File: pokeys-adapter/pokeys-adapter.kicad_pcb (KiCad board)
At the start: 2 copper layers, 19 x 62.9 mm, 7 parts, among them J1 Bus, J2 PinHeader_01x12, J3 PinHeader_01x12, J4 Screw_Terminal_01x02, J5 Mounting hole, J6 Mounting hole

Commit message: Minor artistic changes
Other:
- board text added: "CNC Panel Adapter Hacklab Lahti"

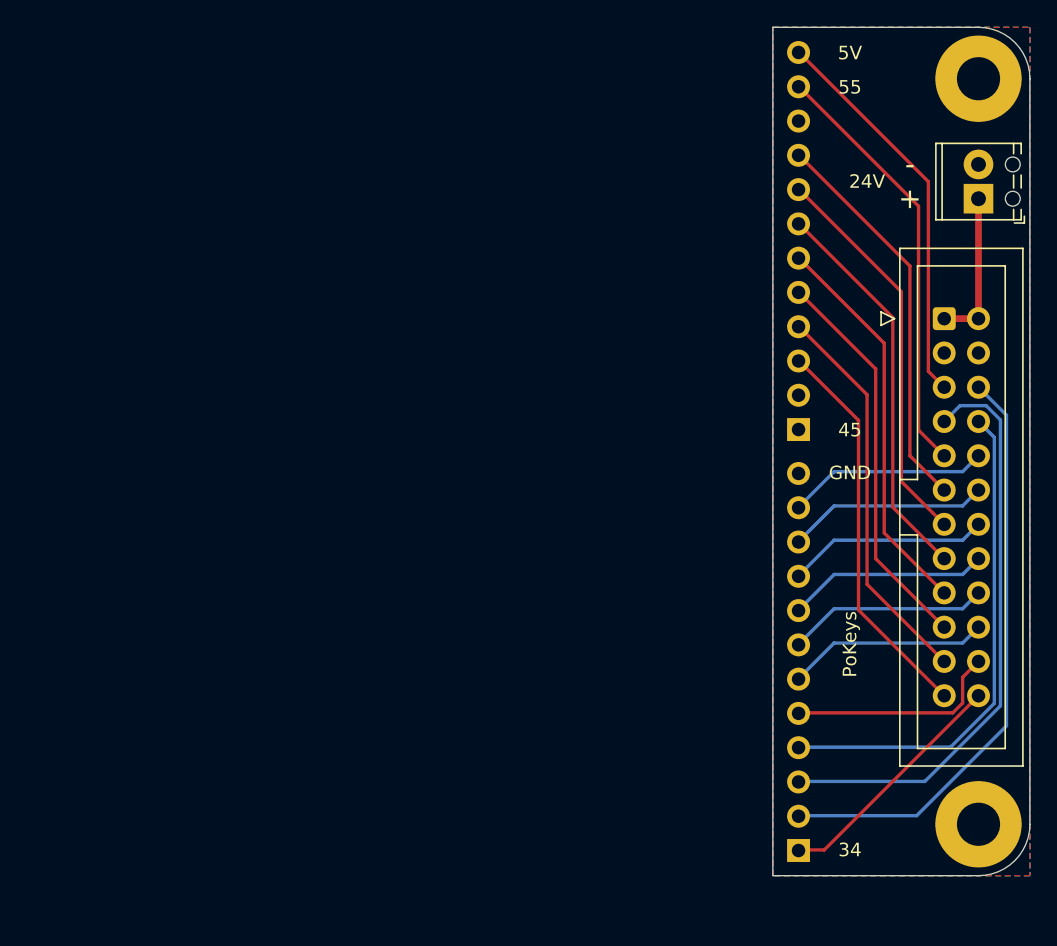
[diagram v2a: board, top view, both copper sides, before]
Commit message: Add level shifters and pullups
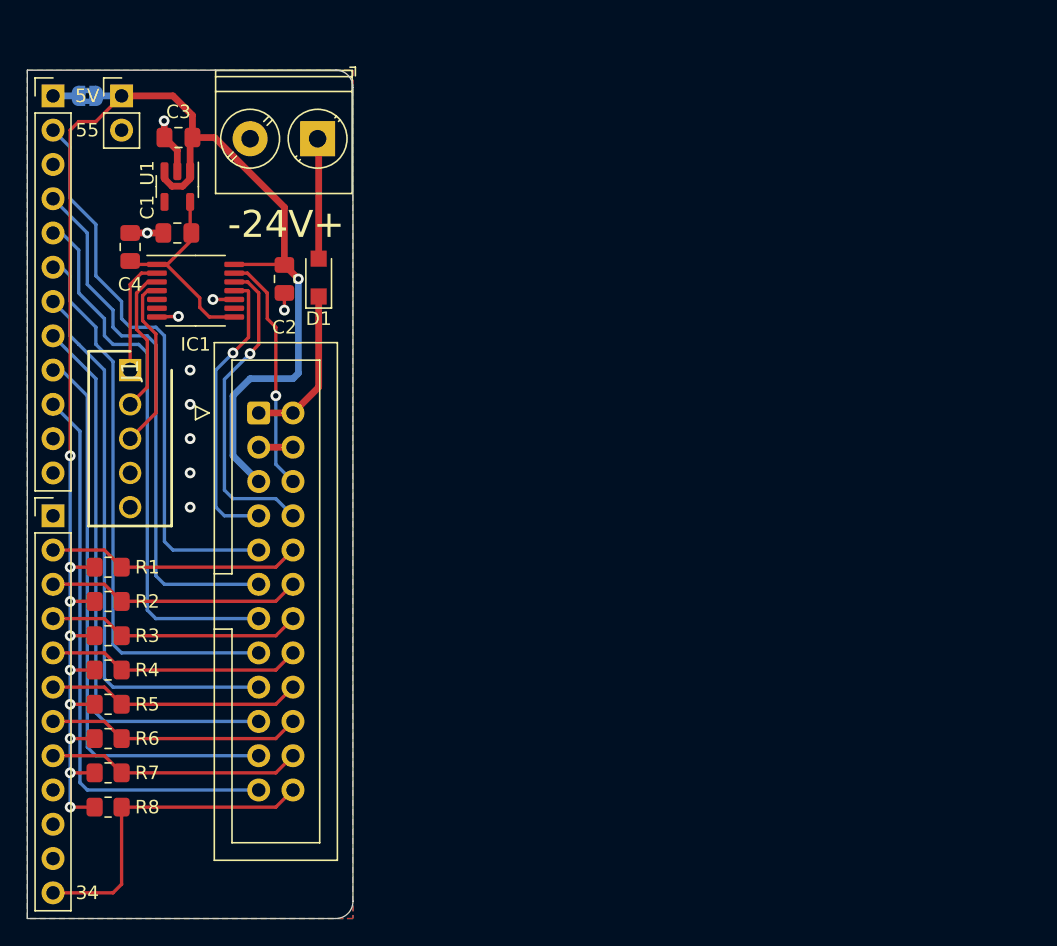
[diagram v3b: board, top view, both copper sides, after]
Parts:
- removed the J5 at (96.5, 22.9)
- removed the J6 at (96.5, 78.1)
- removed REF**: Pokeys56U, Project:Pokeys56U
- added C1: 0.1u, Capacitor_SMD:C_0805_2012Metric_Pad1.18x1.45mm_HandSolder, F.Cu at (33.7, 35.3)
- added C2: 0.1u, Capacitor_SMD:C_0805_2012Metric_Pad1.18x1.45mm_HandSolder, F.Cu at (45.1, 37.7)
- added C3: 1u, Capacitor_SMD:C_0805_2012Metric_Pad1.18x1.45mm_HandSolder, F.Cu at (37.2, 27.2)
- added C4: 1u, Capacitor_SMD:C_0805_2012Metric_Pad1.18x1.45mm_HandSolder, F.Cu at (37.1, 34.3)
- added D1: PMEG3020BER, Diode_SMD:Nexperia_CFP3_SOD-123W, F.Cu at (47.6, 37.6)
- added IC1: TXU0304PWR, Package_SO:TSSOP-14_4.4x5mm_P0.65mm, F.Cu at (38.5, 38.6)
- added J1: 22-27-2051, Project:HDRV5W64P0X254_1X5_1270X580X1205P, F.Cu at (33.7, 44.5)
- added J4: Conn_01x02_Male, Connector_PinHeader_2.54mm:PinHeader_1x02_P2.54mm_Vertical, F.Cu at (33.0, 24.1)
- added JP1: SolderJumper_2_Bridged, Jumper:SolderJumper-2_P1.3mm_Bridged2Bar_RoundedPad1.0x1.5mm, B.Cu at (30.5, 24.1)
- added R1: 1k, Resistor_SMD:R_0805_2012Metric_Pad1.20x1.40mm_HandSolder, F.Cu at (32.0, 59.1)
- added R2: 1k, Resistor_SMD:R_0805_2012Metric_Pad1.20x1.40mm_HandSolder, F.Cu at (32.0, 61.6)
- added R3: 1k, Resistor_SMD:R_0805_2012Metric_Pad1.20x1.40mm_HandSolder, F.Cu at (32.0, 64.1)
- added R4: 1k, Resistor_SMD:R_0805_2012Metric_Pad1.20x1.40mm_HandSolder, F.Cu at (32.0, 66.7)
- added R5: 1k, Resistor_SMD:R_0805_2012Metric_Pad1.20x1.40mm_HandSolder, F.Cu at (32.0, 69.2)
- added R6: 1k, Resistor_SMD:R_0805_2012Metric_Pad1.20x1.40mm_HandSolder, F.Cu at (32.0, 71.8)
- added R7: 1k, Resistor_SMD:R_0805_2012Metric_Pad1.20x1.40mm_HandSolder, F.Cu at (32.0, 74.3)
- added R8: 1k, Resistor_SMD:R_0805_2012Metric_Pad1.20x1.40mm_HandSolder, F.Cu at (32.0, 76.8)
- added U1: MIC5504-3.3YM5, Package_TO_SOT_SMD:SOT-23-5, F.Cu at (37.1, 30.9)
- J2, J3: footprint Project:PinHeader_1x12_P2.54mm_Horizontal_Reversed -> Connector_PinHeader_2.54mm:PinHeader_1x12_P2.54mm_Vertical
- J6: renamed from J4; footprint Project:TerminalBlock_Phoenix_MPT-0,5-2-2.54_1x02_P2.54mm_Horizontal -> TerminalBlock_Phoenix:TerminalBlock_Phoenix_PT-1,5-2-5.0-H_1x02_P5.00mm_Horizontal
- moved J3 60.6 mm to (27.9, 55.2), turned to 0 degrees
- moved J2 60.5 mm to (27.9, 24.1), turned to 0 degrees
- moved J5 51.3 mm to (43.2, 47.6)
- moved J6 49.2 mm to (47.5, 27.3), turned to 180 degrees
- renumbered J1 to J5
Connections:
- J2 pad 10: Net-(J2-Pad10) -> /R8
- J2 pad 11: /R1 -> unconnected-(J2-Pad11)
- J2 pad 12: +5V -> unconnected-(J2-Pad12)
- J2 pad 2: Net-(J2-Pad2) -> /R1
- J2 pad 3: /R8 -> unconnected-(J2-Pad3)
- J2 pad 4: /R7 -> /R2
- J2 pad 5: /R6 -> /R3
- J2 pad 6: /R5 -> /R4
- J2 pad 7: /R4 -> /R5
- J2 pad 8: /R3 -> /R6
- J2 pad 9: /R2 -> /R7
- J3 pad 1: /C8 -> GND
- J3 pad 10: /C2 -> unconnected-(J3-Pad10)
- J3 pad 11: /C1 -> unconnected-(J3-Pad11)
- J3 pad 12: GND -> /C8
- J3 pad 2: /BusClock -> /C1
- J3 pad 3: /BusOut -> /C2
- J3 pad 4: /BusLatch -> /C3
- J3 pad 5: /C7 -> /C4
- J3 pad 6: /C6 -> /C5
- J3 pad 7: /C5 -> /C6
- J3 pad 8: /C4 -> /C7
- J3 pad 9: /C3 -> unconnected-(J3-Pad9)
- J6 pad 1: +24V -> Net-(D1-Pad2)
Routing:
- net +5V: track 29.3 -> 123.0 mm, vias 0 -> 10
- net /BusClock: track 44.1 -> 17.8 mm, vias 0 -> 1
- net /BusOut: track 43.6 -> 21.5 mm, vias 0 -> 1
- net +3V3: track 0.00 -> 15.3 mm
- net GND: track 0.00 -> 13.7 mm, vias 0 -> 10
- net /BusLatch: track 37.2 -> 23.7 mm, vias 0 -> 1
- net /R8: track 29.3 -> 42.3 mm
- net Net-(IC1-Pad4): track 0.00 -> 13.0 mm
- net /R7: track 29.3 -> 41.7 mm
- net /R6: track 29.3 -> 41.6 mm
- net /R5: track 29.3 -> 41.2 mm
- net /R4: track 29.3 -> 40.6 mm
- net Net-(IC1-Pad3): track 0.00 -> 11.0 mm
- net /R3: track 29.3 -> 40.2 mm
- net /R2: track 29.3 -> 40.1 mm
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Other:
- board size 19 x 62.9 mm -> 24.1 x 62.9 mm
- net class Default removed
- board text added: "-24V+"
- board text added: "CNC Panel Adapter 2.0 Hacklab Lahti"
- board text removed: "+"
- board text removed: "-"
- board text removed: "24V"
- board text removed: "45"
- board text removed: "CNC Panel Adapter Hacklab Lahti"
- board text removed: "GND"
- board text removed: "PoKeys"
